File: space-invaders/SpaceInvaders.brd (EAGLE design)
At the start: 101.6 x 95.2 mm, 26 parts, among them J2-J4 TM4C123GXL, J3-J1 TM4C123GXL, J5 NOKIA_5110, J6 NOKIA_5110, J7 9V, U1 LM7805CT

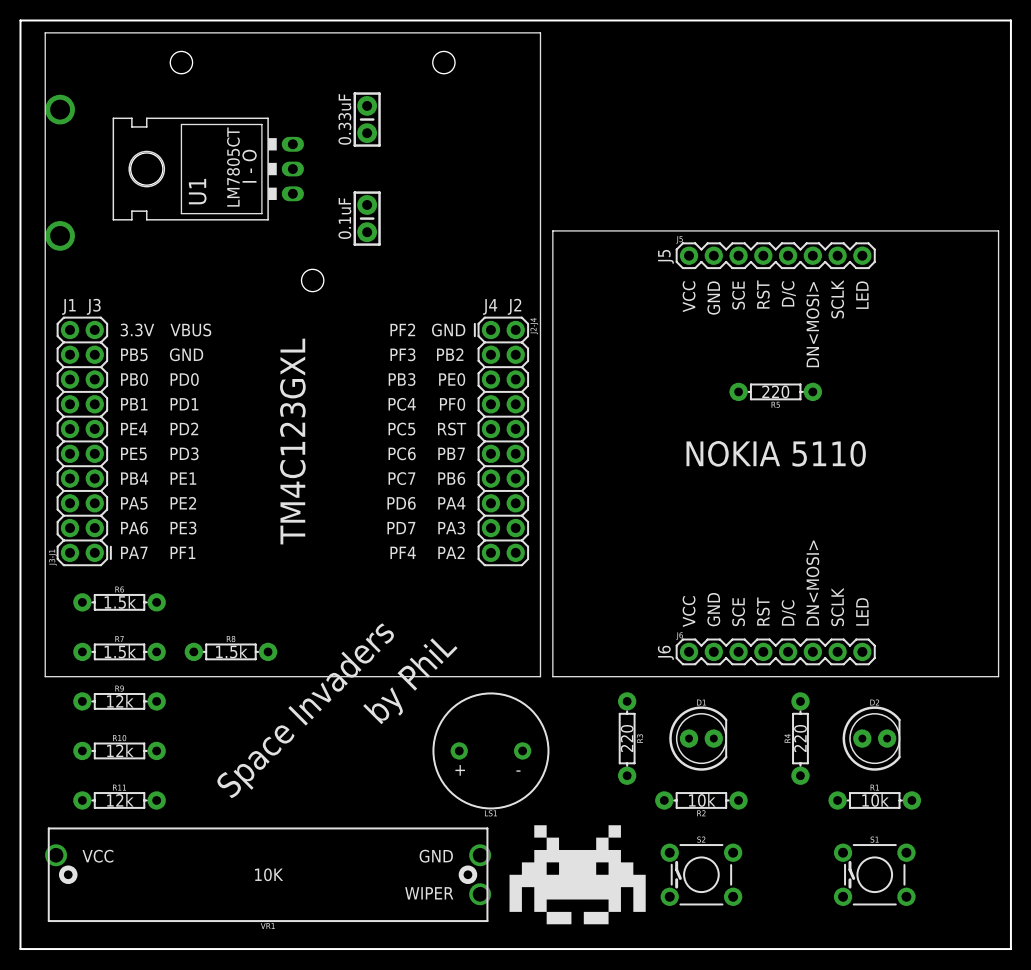
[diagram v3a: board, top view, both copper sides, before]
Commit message: Route SpaceInvaders Manually - SpaceInvaders v3.0
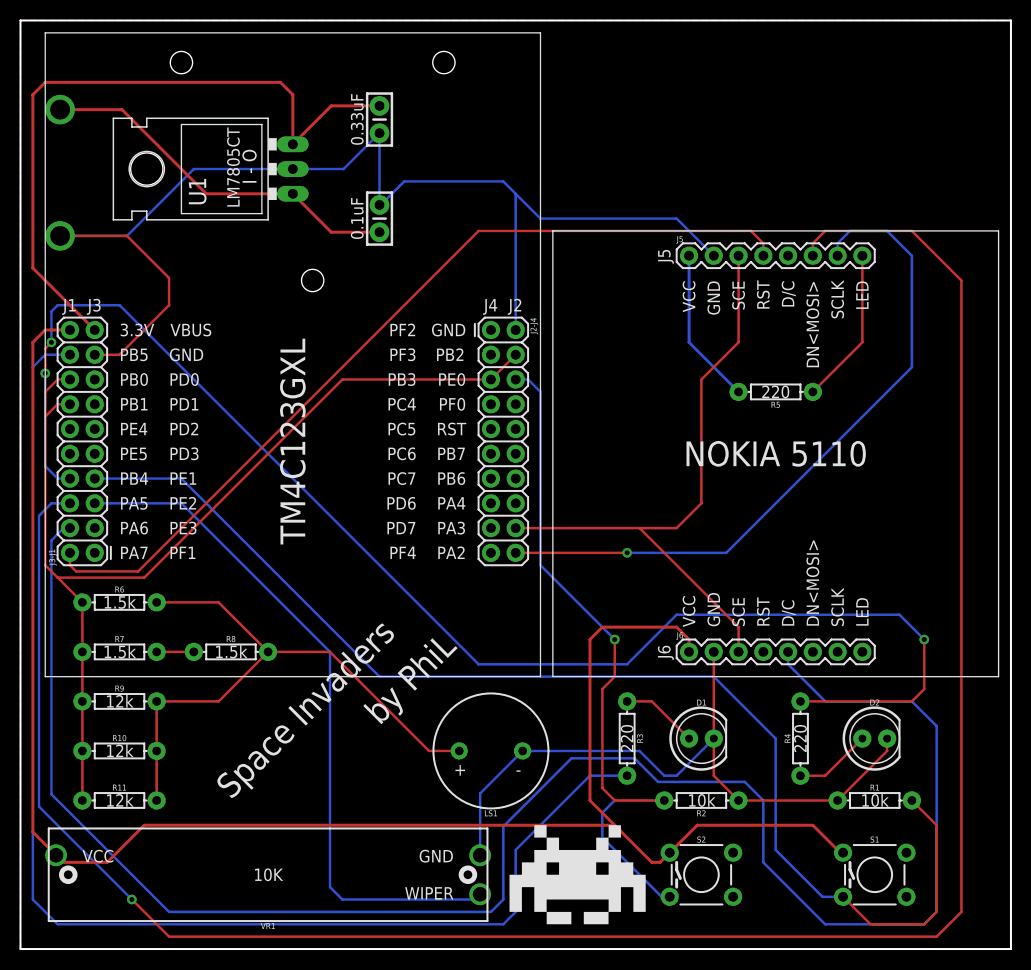
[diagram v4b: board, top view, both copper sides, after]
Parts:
- moved C1 1.27 mm to (36.8, 85.1)
- moved C2 1.27 mm to (36.8, 74.9)
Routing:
- net PA5: track 0.00 -> 218.6 mm, vias 0 -> 1
- net 3.3V: track 0.00 -> 193.5 mm
- net GND: track 0.00 -> 192.2 mm
- net PA6: track 0.00 -> 184.7 mm
- net PB4: track 0.00 -> 145.7 mm, vias 0 -> 3
- net PB5: track 0.00 -> 131.0 mm
- net PE1: track 0.00 -> 125.0 mm
- net DAC: track 0.00 -> 106.1 mm
- net PA7: track 0.00 -> 88.9 mm
- net PE0: track 0.00 -> 73.1 mm, vias 0 -> 1
- net PE2: track 0.00 -> 70.7 mm
- net PA2: track 0.00 -> 70.4 mm, vias 0 -> 1
- net VBUS: track 0.00 -> 70.1 mm
- net PA3: track 0.00 -> 64.0 mm
- net DAC_OUT: track 0.00 -> 61.0 mm
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- added copper zone on layer 1, net GND

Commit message: Minimize the board area to 3.60" x 3.60"
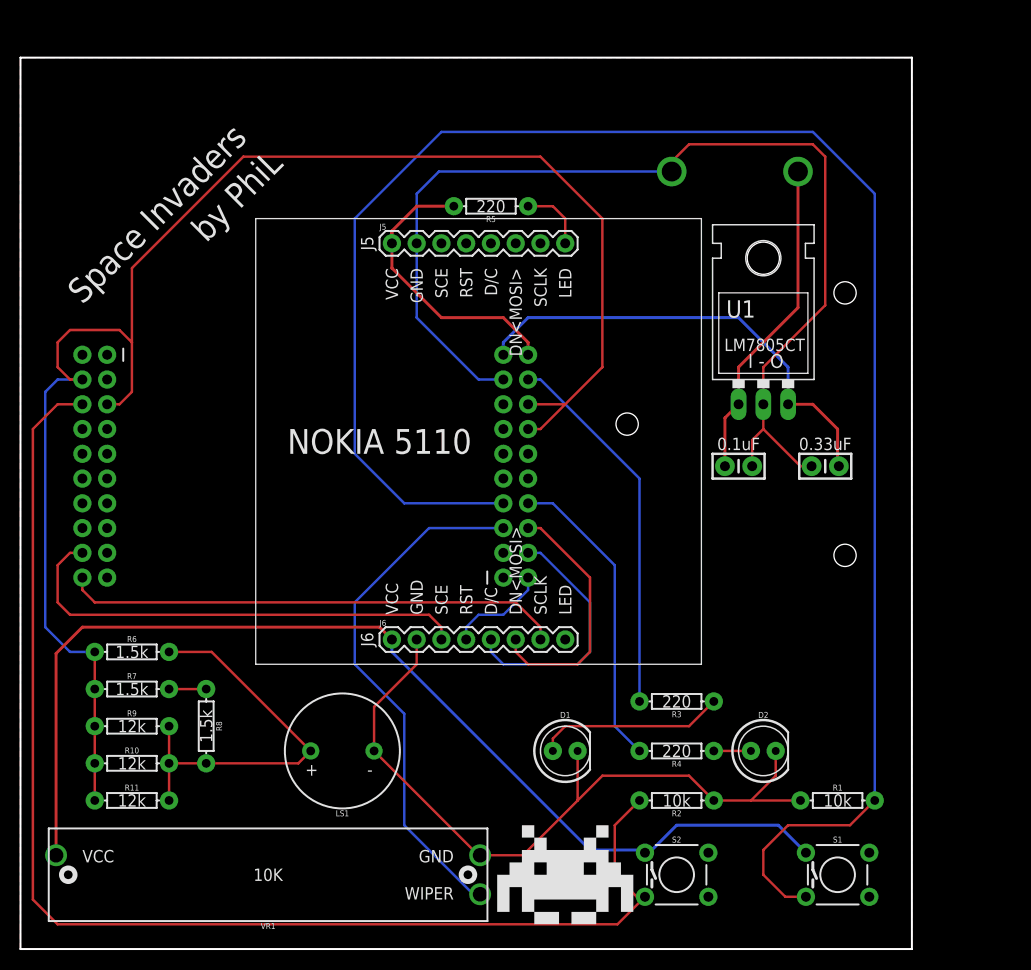
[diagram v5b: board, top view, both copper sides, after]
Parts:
- moved C1 57.9 mm to (82.5, 49.5), turned to 0 degrees
- moved U1 55.9 mm to (76.2, 59.7), turned to 0 degrees
- moved C2 44.7 mm to (73.7, 49.5), turned to 0 degrees
- moved J3-J1 42.0 mm to (49.5, 38.1), flipped to the bottom
- moved J2-J4 39.5 mm to (8.89, 61.0), flipped to the bottom
- moved J7 38.1 mm to (58.4, 26.7), turned to 90 degrees
- moved R5 34.9 mm to (48.3, 76.2)
- moved J5 30.5 mm to (38.1, 72.4)
- moved J6 30.5 mm to (38.1, 31.8)
- moved LS1 15.2 mm to (33.0, 20.3)
- moved D1 14.0 mm to (55.9, 20.3)
- moved R4 12.8 mm to (67.3, 20.3), turned to 180 degrees
- moved D2 11.5 mm to (76.2, 20.3)
- moved R8 8.03 mm to (19.1, 22.9), turned to 270 degrees
- moved R3 6.35 mm to (67.3, 25.4), turned to 180 degrees
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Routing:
- net PA5: track 218.6 -> 26.0 mm, vias 1 -> 0
- net PA6: track 184.7 -> 26.0 mm
- net PB4: track 145.7 -> 31.6 mm, vias 3 -> 0
- net PB5: track 131.0 -> 38.5 mm
- net PA7: track 88.9 -> 10.5 mm
- net PE1: track 125.0 -> 184.7 mm
- net PE0: track 73.1 -> 132.1 mm, vias 1 -> 0
- net DAC: track 106.1 -> 164.8 mm
- net 3.3V: track 193.5 -> 142.3 mm
- net VBUS: track 70.1 -> 47.4 mm
- net DAC_OUT: track 61.0 -> 41.4 mm
- net PA2: track 70.4 -> 51.1 mm, vias 1 -> 0
- net PE2: track 70.7 -> 54.1 mm
- net PA3: track 64.0 -> 48.6 mm
- net LLED: track 7.93 -> 19.4 mm
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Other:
- board size 101.6 x 95.2 mm -> 91.4 x 91.4 mm
